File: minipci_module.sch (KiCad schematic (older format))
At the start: 1 part, among them Con3 2041119-1

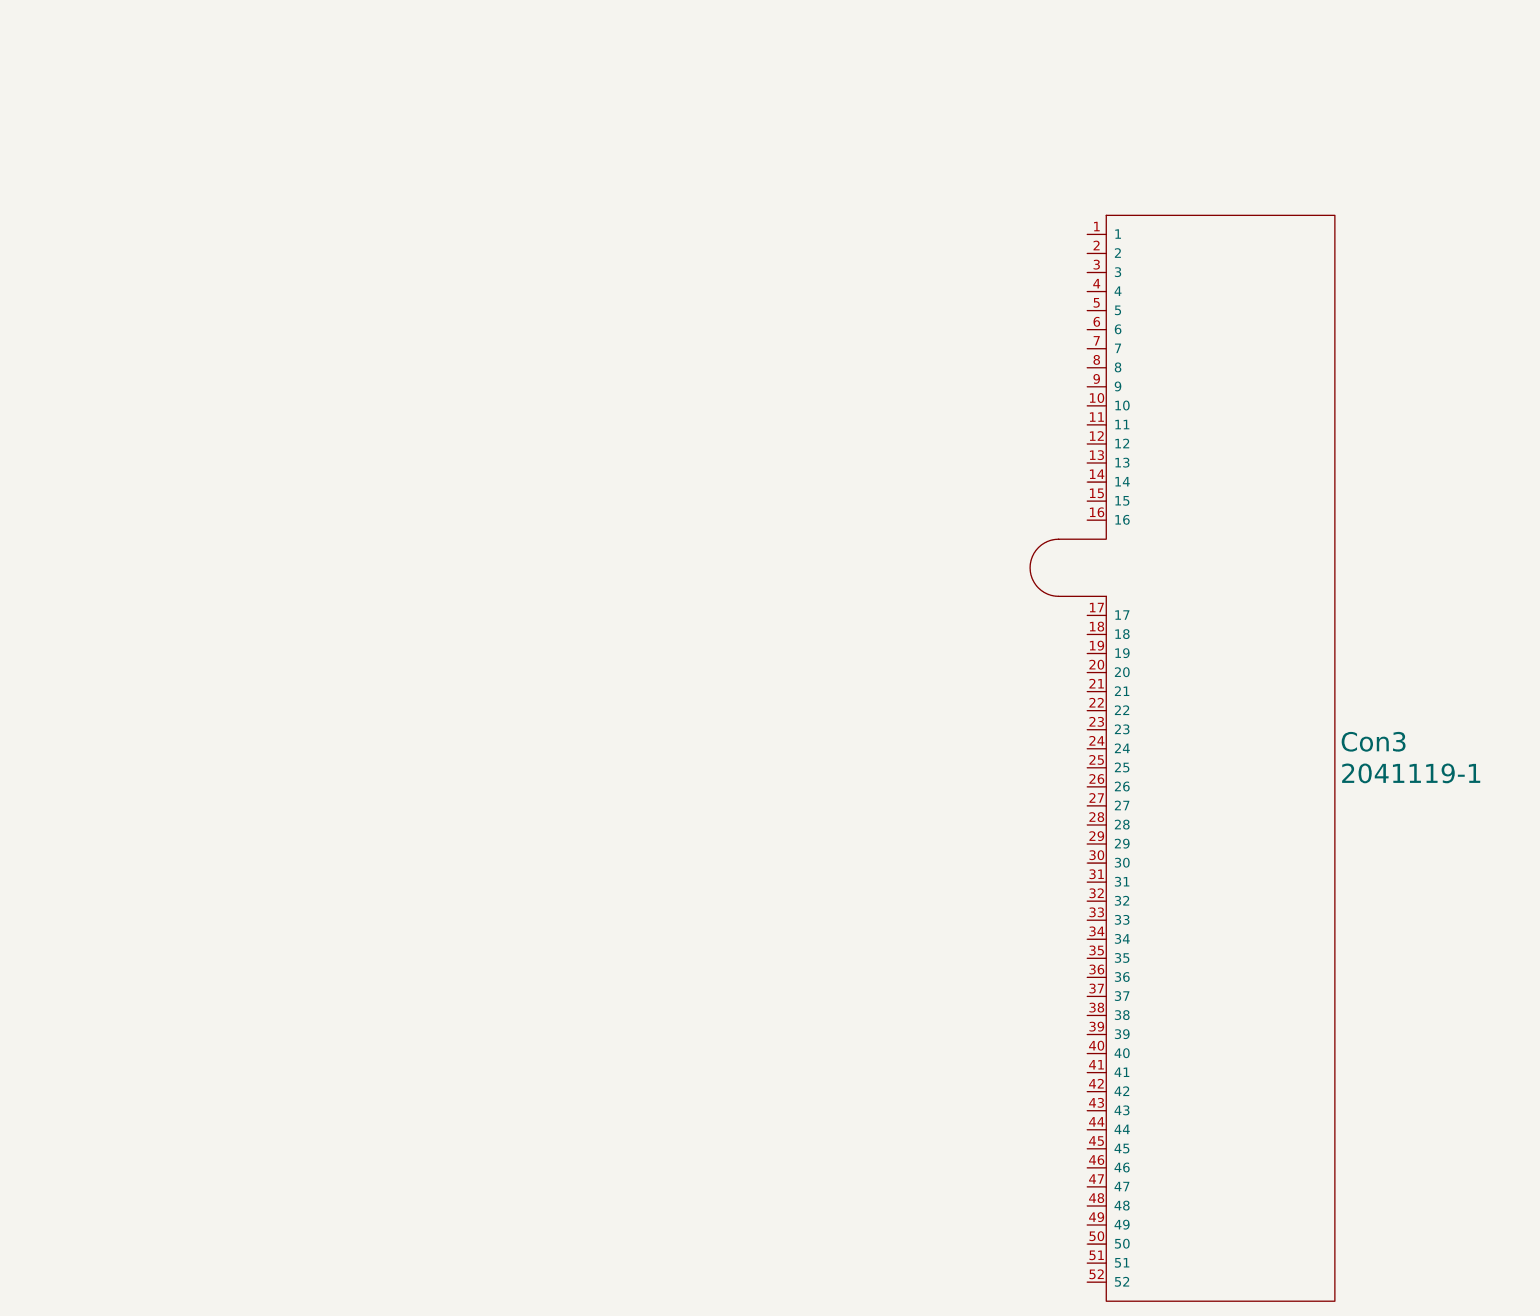
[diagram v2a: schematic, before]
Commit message: Schematic work contiune, added pinout spreadsheet
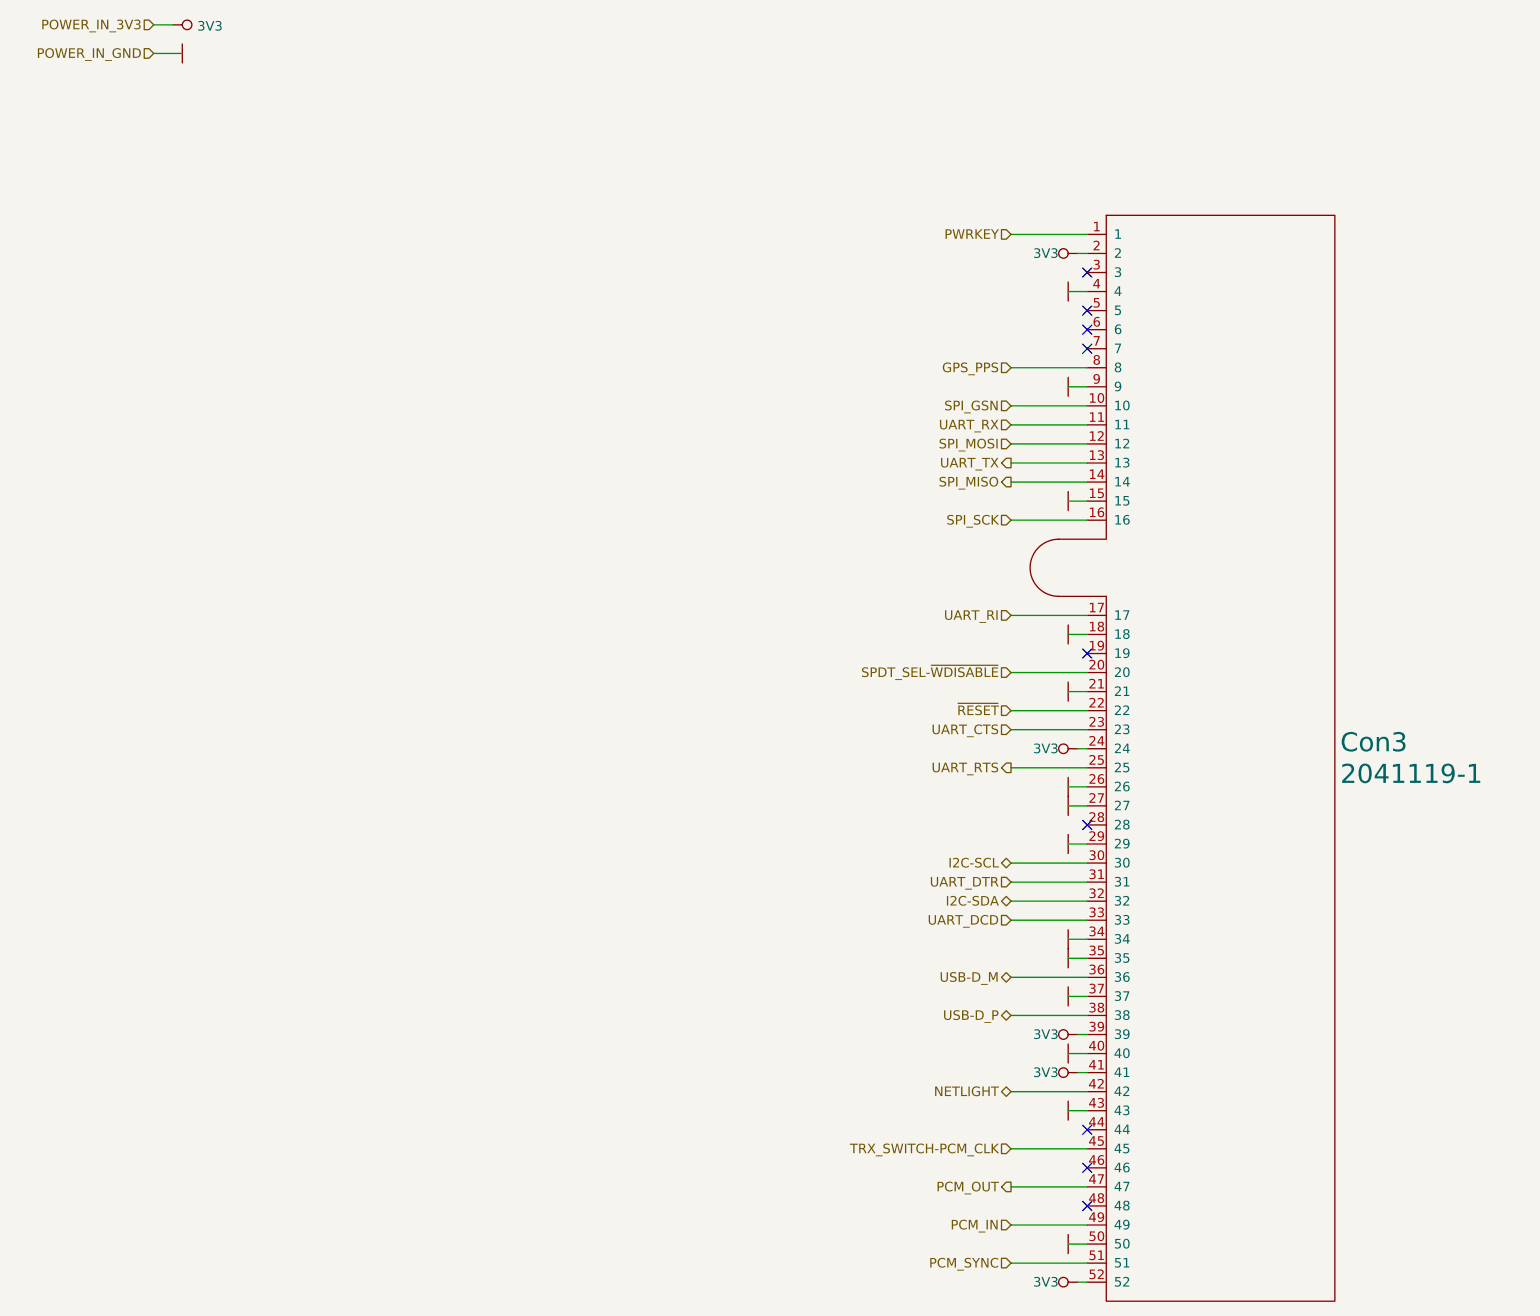
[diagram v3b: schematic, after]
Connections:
- net PWRKEY: now reaches Con3.1
- net SPI_GSN: now reaches Con3.10
- net UART_RX: now reaches Con3.11
- net SPI_MOSI: now reaches Con3.12
- net UART_TX: now reaches Con3.13
- net SPI_MISO: now reaches Con3.14
- net GND: now reaches Con3.15
- net GND: now also Con3.18, Con3.21, Con3.26, Con3.27, Con3.29, Con3.34, Con3.35, Con3.37, Con3.4, Con3.40, Con3.43, Con3.50, Con3.9
- net SPI_SCK: now reaches Con3.16
- net UART_RI: now reaches Con3.17
- net 3V3: now reaches Con3.2
- net 3V3: now also Con3.24, Con3.39, Con3.41, Con3.52
- net SPDT_SEL-~WDISABLE~: now reaches Con3.20
- net ~RESET~: now reaches Con3.22
- net UART_CTS: now reaches Con3.23
- net UART_RTS: now reaches Con3.25
- net I2C-SCL: now reaches Con3.30
- net UART_DTR: now reaches Con3.31
- net I2C-SDA: now reaches Con3.32
- net UART_DCD: now reaches Con3.33
- net USB-D_M: now reaches Con3.36
- net USB-D_P: now reaches Con3.38
- net NETLIGHT: now reaches Con3.42
- net TRX_SWITCH-PCM_CLK: now reaches Con3.45
- net PCM_OUT: now reaches Con3.47
- net PCM_IN: now reaches Con3.49
- net PCM_SYNC: now reaches Con3.51
- net GPS_PPS: now reaches Con3.8
- no-connect marks 0 -> 9

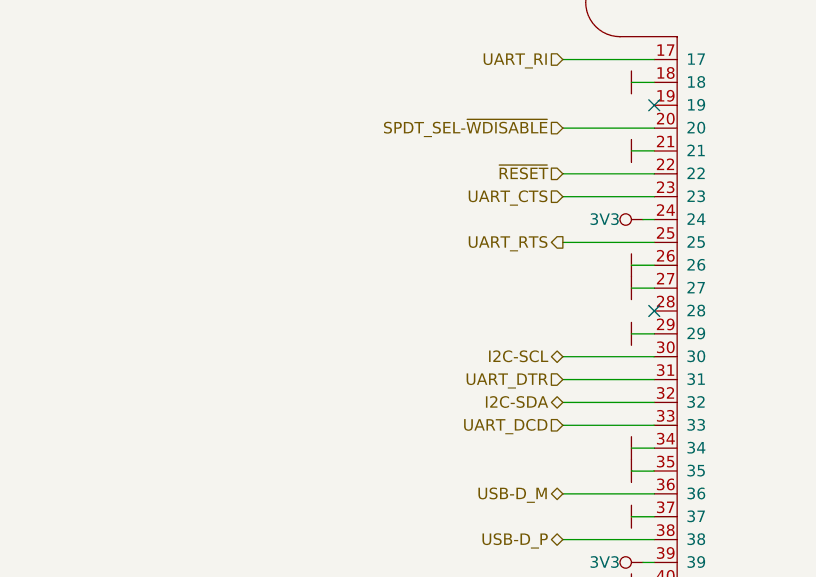
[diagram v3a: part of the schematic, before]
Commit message: Added missing components like LED diodes, i2c pull-up resistors
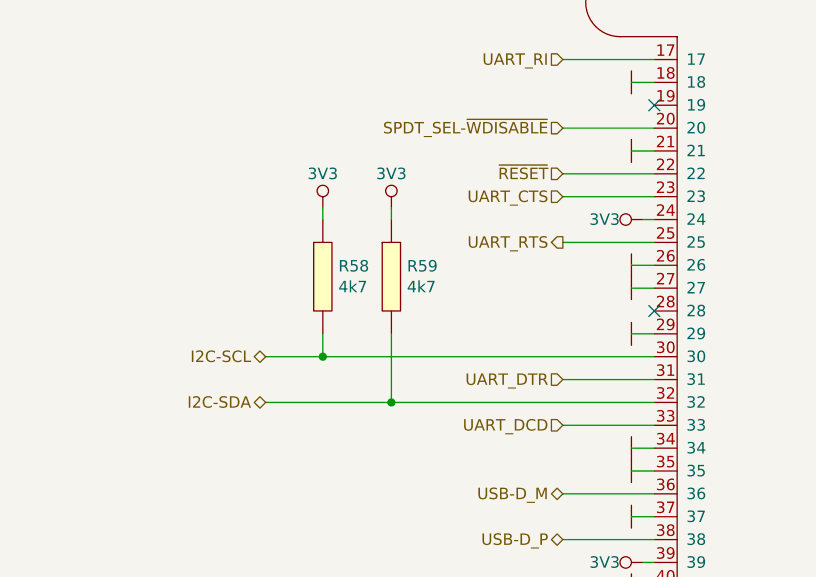
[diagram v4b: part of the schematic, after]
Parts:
- added R58, R59: 4k7, Resistor_Smd_0603:4k7_0603, symbol Resistors_Smd0603:4k7
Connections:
- net 3V3: now also R58.1, R59.1
- net I2C-SCL: now also R58.2
- net I2C-SDA: now also R59.2
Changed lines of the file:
@@
 Wire Wire Line
 	7450 5200 7050 5200
-Text HLabel 7050 6000 0    50   BiDi ~ 0
+Text HLabel 5750 6000 0    50   BiDi ~ 0
 I2C-SCL
 Wire Wire Line
-	7450 6000 7050 6000
-Text HLabel 7050 6200 0    50   BiDi ~ 0
+	7450 6000 6000 6000
+Text HLabel 5750 6200 0    50   BiDi ~ 0
 I2C-SDA
 Wire Wire Line
-	7450 6200 7050 6200
+	7450 6200 6300 6200
 Text HLabel 7050 7200 0    50   BiDi ~ 0
 NETLIGHT
@@
 	0    1    1    0
 $EndComp
+$Comp
+L Resistors_Smd0603:4k7 R?
+U 1 1 60112A2F
+P 6000 5650
+AR Path="/5FDE4F7C/60112A2F" Ref="R?"  Part="1"
+AR Path="/5FFEC95A/60112A2F" Ref="R58"  Part="1"
+F 0 "R58" H 6068 5696 50  0000 L CNN
+F 1 "4k7" H 6068 5605 50  0000 L CNN
+F 2 "Resistor_Smd_0603:4k7_0603" H 6000 5650 50  0001 C CNN
+F 3 "Resistors/Smd_0603/Components_Documentation/Vishay_Resistors_SM0603.pdf" H 6000 5650 50  0001 C CNN
+F 4 "ROYAL OHM" H 6000 5650 50  0001 C CNN "Manufacturer"
+F 5 "0603SAF4701T5E" H 6000 5650 50  0001 C CNN "Manufacturer Part Number"
+F 6 "TME" H 6000 5650 50  0001 C CNN "Supplier"
+F 7 "	SMD0603-4K7-1%" H 6000 5650 50  0001 C CNN "Supplier Part Number"
+F 8 "https://www.tme.eu/pl/details/smd0603-4k7-1%2525/rezystory-smd-0603/royal-ohm/0603saf4701t5e/" H 6000 5650 50  0001 C CNN "URL"
+F 9 "0,04698" H 6000 5650 50  0001 C CNN "Price@1pc"
+F 10 "0,01271" H 6000 5650 50  0001 C CNN "Price@1000pcs"
+F 11 "0603" H 6000 5650 50  0001 C CNN "Package"
+	1    6000 5650
+	1    0    0    -1
+$EndComp
+$Comp
+L power:3V3_NO_GLOBAL #PWR?
+U 1 1 60112A35
+P 6000 5350
+AR Path="/5FDE4F7C/60112A35" Ref="#PWR?"  Part="1"
+AR Path="/5FFEC95A/60112A35" Ref="#PWR199"  Part="1"
+F 0 "#PWR199" H 6000 5450 40  0001 C CNN
+F 1 "3V3" H 6000 5500 50  0000 C CNN
+F 2 "" H 6000 5350 60  0000 C CNN
+F 3 "" H 6000 5350 60  0000 C CNN
+	1    6000 5350
+	1    0    0    -1
+$EndComp
+Wire Wire Line
+	6000 5350 6000 5400
+$Comp
+L Resistors_Smd0603:4k7 R?
+U 1 1 60115664
+P 6300 5650
+AR Path="/5FDE4F7C/60115664" Ref="R?"  Part="1"
+AR Path="/5FFEC95A/60115664" Ref="R59"  Part="1"
+F 0 "R59" H 6368 5696 50  0000 L CNN
+F 1 "4k7" H 6368 5605 50  0000 L CNN
+F 2 "Resistor_Smd_0603:4k7_0603" H 6300 5650 50  0001 C CNN
+F 3 "Resistors/Smd_0603/Components_Documentation/Vishay_Resistors_SM0603.pdf" H 6300 5650 50  0001 C CNN
+F 4 "ROYAL OHM" H 6300 5650 50  0001 C CNN "Manufacturer"
+F 5 "0603SAF4701T5E" H 6300 5650 50  0001 C CNN "Manufacturer Part Number"
+F 6 "TME" H 6300 5650 50  0001 C CNN "Supplier"
+F 7 "	SMD0603-4K7-1%" H 6300 5650 50  0001 C CNN "Supplier Part Number"
+F 8 "https://www.tme.eu/pl/details/smd0603-4k7-1%2525/rezystory-smd-0603/royal-ohm/0603saf4701t5e/" H 6300 5650 50  0001 C CNN "URL"
+F 9 "0,04698" H 6300 5650 50  0001 C CNN "Price@1pc"
+F 10 "0,01271" H 6300 5650 50  0001 C CNN "Price@1000pcs"
+F 11 "0603" H 6300 5650 50  0001 C CNN "Package"
+	1    6300 5650
+	1    0    0    -1
+$EndComp
+$Comp
+L power:3V3_NO_GLOBAL #PWR?
+U 1 1 6011581A
+P 6300 5350
+AR Path="/5FDE4F7C/6011581A" Ref="#PWR?"  Part="1"
+AR Path="/5FFEC95A/6011581A" Ref="#PWR200"  Part="1"
+F 0 "#PWR200" H 6300 5450 40  0001 C CNN
+F 1 "3V3" H 6300 5500 50  0000 C CNN
+F 2 "" H 6300 5350 60  0000 C CNN
+F 3 "" H 6300 5350 60  0000 C CNN
+	1    6300 5350
+	1    0    0    -1
+$EndComp
+Wire Wire Line
+	6300 5350 6300 5400
+Wire Wire Line
+	6300 5900 6300 6200
+Connection ~ 6300 6200
+Wire Wire Line
+	6300 6200 5750 6200
+Wire Wire Line
+	6000 5900 6000 6000
+Connection ~ 6000 6000
+Wire Wire Line
+	6000 6000 5750 6000
 $EndSCHEMATC
